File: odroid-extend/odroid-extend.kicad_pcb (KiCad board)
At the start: 2 copper layers, 58.4 x 65.5 mm, 7 parts, among them J1 Conn_02x20_Odd_Even, J2 Conn_01x20_Male, J3 Conn_01x20_Male, J4 Conn_01x02_Male, J5 Conn_01x02_Male, J6 Conn_01x02_Male, J7 Conn_01x02_Male

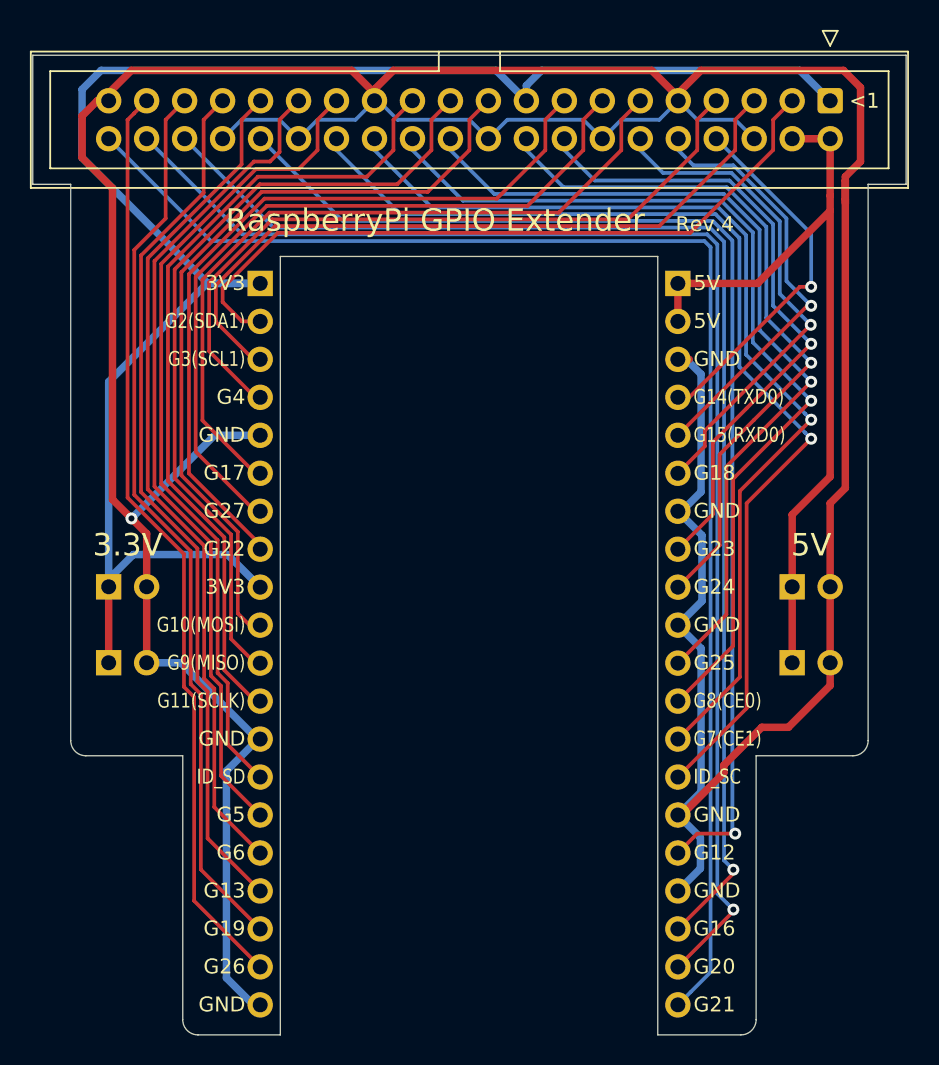
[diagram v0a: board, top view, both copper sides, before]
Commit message: 오드로이드n2용 io 확장보드 추가
Signed-off-by: Ju, Gyeong-min <jcmh74@gmail.com>
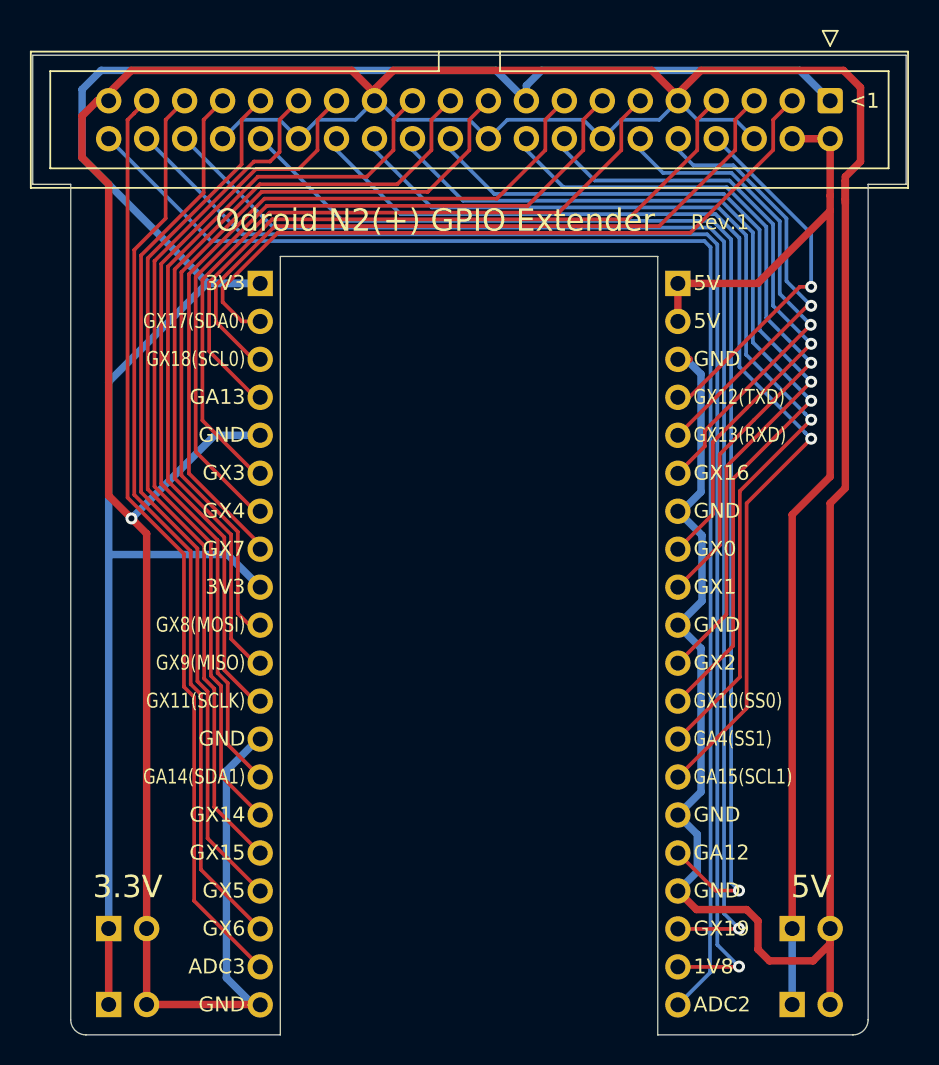
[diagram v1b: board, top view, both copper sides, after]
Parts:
- moved J4 22.9 mm to (138.7, 121.9)
- moved J5 22.9 mm to (184.4, 121.9)
- moved J6 22.9 mm to (138.7, 127.0)
- moved J7 22.9 mm to (184.4, 127.0)
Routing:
- net GND: track 278.3 -> 320.9 mm
- net +5V: track 53.9 -> 76.7 mm
- net +3V3: track 117.5 -> 139.7 mm
- net Net-(J1-Pad32): track 78.7 -> 83.4 mm
- net Net-(J1-Pad38): track 91.4 -> 94.1 mm
- net Net-(J1-Pad36): track 86.7 -> 89.4 mm
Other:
- outline, holes or cut-outs redrawn
- board text added: "1V8"
- board text added: "ADC2"
- board text added: "ADC3"
- board text added: "GA12"
- board text added: "GA13"
- board text added: "GA14(SDA1)"
- board text added: "GA15(SCL1)"
- board text added: "GA4(SS1)"
- board text added: "GX0"
- board text added: "GX1"
- board text added: "GX10(SS0)"
- board text added: "GX11(SCLK)"
- board text added: "GX12(TXD)"
- board text added: "GX13(RXD)"
- board text added: "GX14"
- board text added: "GX15"
- board text added: "GX16"
- board text added: "GX17(SDA0)"
- board text added: "GX18(SCL0)"
- board text added: "GX19"
- board text added: "GX2"
- board text added: "GX3"
- board text added: "GX4"
- board text added: "GX5"
- board text added: "GX6"
- board text added: "GX7"
- board text added: "GX8(MOSI)"
- board text added: "GX9(MISO)"
- board text added: "Odroid N2(+) GPIO Extender"
- board text added: "Rev.1"
- board text removed: "G10(MOSI)"
- board text removed: "G11(SCLK)"
- board text removed: "G12"
- board text removed: "G13"
- board text removed: "G14(TXD0)"
- board text removed: "G15(RXD0)"
- board text removed: "G16"
- board text removed: "G17"
- board text removed: "G18"
- board text removed: "G19"
- board text removed: "G2(SDA1)"
- board text removed: "G20"
- board text removed: "G21"
- board text removed: "G22"
- board text removed: "G23"
- board text removed: "G24"
- board text removed: "G25"
- board text removed: "G26"
- board text removed: "G27"
- board text removed: "G3(SCL1)"
- board text removed: "G4"
- board text removed: "G5"
- board text removed: "G6"
- board text removed: "G7(CE1)"
- board text removed: "G8(CE0)"
- board text removed: "G9(MISO)"
- board text removed: "ID_SC"
- board text removed: "ID_SD"
- board text removed: "RaspberryPi GPIO Extender"
- board text removed: "Rev.4"
